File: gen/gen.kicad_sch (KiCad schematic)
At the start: 16 parts

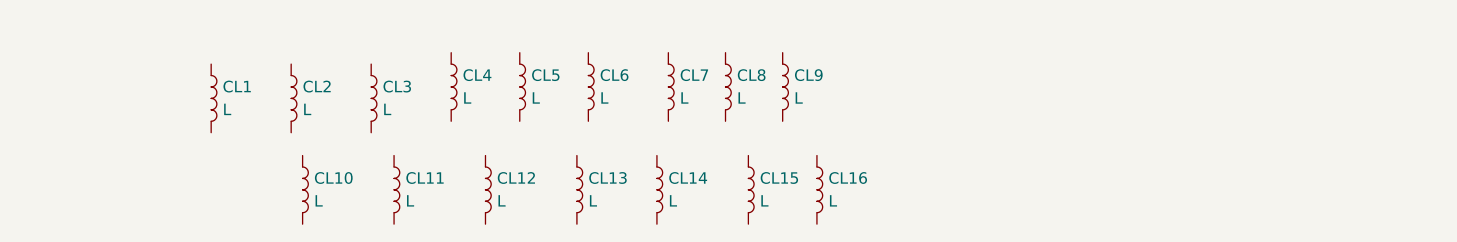
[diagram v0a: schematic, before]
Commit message: Connected All Coils
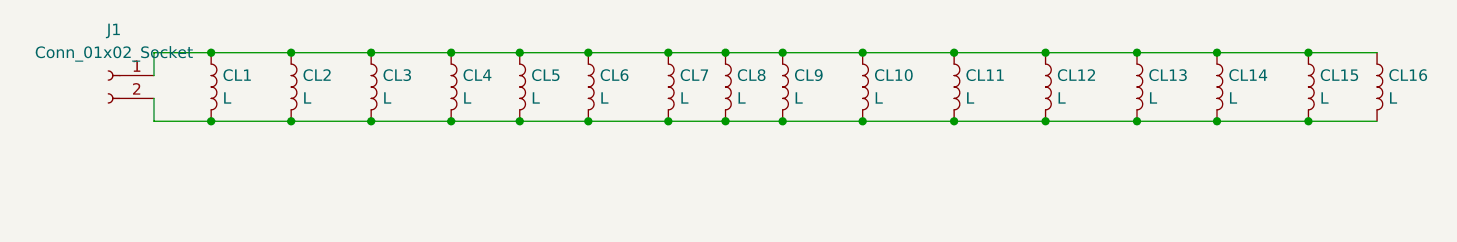
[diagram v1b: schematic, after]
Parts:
- added J1: Conn_01x02_Socket, Connector_PinHeader_2.54mm:PinHeader_1x02_P2.54mm_Vertical, symbol Connector:Conn_01x02_Socket
- CL1, CL10, CL11, CL12, CL13, CL14, CL15, CL16, CL2, CL3, CL4, CL5, CL6, CL7, CL8, CL9: footprint (none) -> PCB Coils:SMALL_COIL
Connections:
- net at CL5.1: now also CL1.1, CL10.1, CL11.1, CL12.1, CL13.1, CL14.1, CL15.1, CL16.1, CL2.1, CL3.1, CL4.1, CL6.1, CL7.1, CL8.1, CL9.1, J1.1 (Pin_1)
- net at CL5.2: now also CL1.2, CL10.2, CL11.2, CL12.2, CL13.2, CL14.2, CL15.2, CL16.2, CL2.2, CL3.2, CL4.2, CL6.2, CL7.2, CL8.2, CL9.2, J1.2 (Pin_2)
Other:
- moved on the sheet: CL1, CL10, CL11, CL12, CL13, CL14, CL15, CL16, CL2, CL3
